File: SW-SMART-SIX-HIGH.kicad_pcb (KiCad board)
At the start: 2 copper layers, 107.7 x 76.2 mm, 97 parts, among them J1 SWLINK, J2 USART2, J3 POWER OUT, J4 POWER IN, J5 POWER OUT, SW0 BTS7002-1EPP, SW1 BTS7002-1EPP, SW2 BTS7002-1EPP, SW3 BTS7002-1EPP, SW4 BTS7002-1EPP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

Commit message: fine tune a few things
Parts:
- J1: value SWLINK -> SWD
- moved CIN2 6.40 mm to (94.2, 83.0), turned to 0 degrees
- moved CIN1 5.70 mm to (93.8, 85.4), turned to 0 degrees
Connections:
- C3V1 pad 1: +3.3V -> Net-(U4-Vio)
- D3 pad 2: /STAT2 -> unconnected-(D3-A-Pad2)
- U4 pad 5: +3.3V -> Net-(U4-Vio)
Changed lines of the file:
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@@
 	(net 132 "/STAT2")
 	(net 133 "Net-(D3-K)")
+	(net 134 "Net-(U4-Vio)")
+	(net 135 "unconnected-(D3-A-Pad2)")
 	(footprint "TerminalBlock_Phoenix:TerminalBlock_Phoenix_MKDS-3-5-5.08_1x05_P5.08mm_Horizontal"
 		(layer "F.Cu")
@@
 	(footprint "Capacitor_SMD:C_1210_3225Metric_Pad1.33x2.70mm_HandSolder"
 		(layer "F.Cu")
-		(at 90.95 80.4375 90)
+		(at 93.7625 85.4)
 		(descr "Capacitor SMD 1210 (3225 Metric), square (rectangular) end terminal, IPC-7351 nominal with elongated pad for handsoldering. (Body size source: IPC-SM-782 page 76, https://www.pcb-3d.com/wordpress/wp-content/uploads/ipc-sm-782a_amendment_1_and_2.pdf), generated with kicad-footprint-generator")
 		(tags "capacitor handsolder")
 		(property "Reference" "CIN1"
-			(at 4.1 0.2 90)
+			(at 0.375 2.2 0)
 			(layer "F.SilkS")
 			(effects
@@
 		)
 		(property "Value" "10u"
-			(at 0 2.3 90)
+			(at 0 2.3 0)
 			(layer "F.Fab")
 			(hide yes)
@@
 		)
 		(property "Datasheet" "~"
-			(at 0 0 90)
+			(at 0 0 0)
 			(layer "F.Fab")
 			(hide yes)
@@
 		)
 		(property "Description" "10uf / 50v"
-			(at 0 0 90)
+			(at 0 0 0)
 			(layer "F.Fab")
 			(hide yes)
@@
 		)
 		(fp_text user "${REFERENCE}"
-			(at 0 0 90)
+			(at 0 0 0)
 			(layer "F.Fab")
 			(effects
@@
 		)
 		(pad "1" smd roundrect
-			(at -1.5625 0 90)
+			(at -1.5625 0)
 			(size 1.325 2.7)
 			(layers "F.Cu" "F.Mask" "F.Paste")
@@
 		)
 		(pad "2" smd roundrect
-			(at 1.5625 0 90)
+			(at 1.5625 0)
 			(size 1.325 2.7)
 			(layers "F.Cu" "F.Mask" "F.Paste")
@@
 		(tags "LQFP QFP")
 		(property "Reference" "U1"
-			(at 0 -7.4 0)
+			(at -7.05 -4.7 0)
 			(layer "F.SilkS")
 			(effects
@@
 		(property "Value" "H GND L"
 			(at 5.035 5.683157 0)
-			(layer "F.Fab")
-			(hide yes)
+			(layer "F.SilkS")
 			(effects
 				(font
@@
 			(layers "F.Cu" "F.Mask" "F.Paste")
 			(roundrect_rratio 0.217391)
-			(net 132 "/STAT2")
+			(net 135 "unconnected-(D3-A-Pad2)")
 			(pinfunction "A")
 			(pintype "passive")
@@
 	(footprint "Capacitor_SMD:C_0603_1608Metric_Pad1.08x0.95mm_HandSolder"
 		(layer "F.Cu")
-		(at 88.55 80 90)
+		(at 94.2 83)
 		(descr "Capacitor SMD 0603 (1608 Metric), square (rectangular) end terminal, IPC-7351 nominal with elongated pad for handsoldering. (Body size source: IPC-SM-782 page 76, https://www.pcb-3d.com/wordpress/wp-content/uploads/ipc-sm-782a_amendment_1_and_2.pdf), generated with kicad-footprint-generator")
 		(tags "capacitor handsolder")
 		(property "Reference" "CIN2"
-			(at -0.0625 -1.1 90)
+			(at -0.0625 -1.3 0)
 			(layer "F.SilkS")
 			(effects
@@
 		)
 		(property "Value" "100n"
-			(at 0 1.43 90)
+			(at 0 1.43 0)
 			(layer "F.Fab")
 			(hide yes)
@@
 		)
 		(property "Datasheet" "~"
-			(at 0 0 90)
+			(at 0 0 0)
 			(layer "F.Fab")
 			(hide yes)
@@
 		)
 		(property "Description" "100n / 100v"
-			(at 0 0 90)
+			(at 0 0 0)
 			(layer "F.Fab")
 			(hide yes)
@@
 		)
 		(fp_text user "${REFERENCE}"
-			(at 0 0 90)
+			(at 0 0 0)
 			(layer "F.Fab")
 			(effects
@@
 		)
 		(pad "1" smd roundrect
-			(at -0.8625 0 90)
+			(at -0.8625 0)
 			(size 1.075 0.95)
 			(layers "F.Cu" "F.Mask" "F.Paste")
@@
 		)
 		(pad "2" smd roundrect
-			(at 0.8625 0 90)
+			(at 0.8625 0)
 			(size 1.075 0.95)
 			(layers "F.Cu" "F.Mask" "F.Paste")
@@
 			(layers "F.Cu" "F.Mask" "F.Paste")
 			(roundrect_rratio 0.25)
-			(net 2 "+3.3V")
+			(net 134 "Net-(U4-Vio)")
 			(pinfunction "Vio")
 			(pintype "power_in")
@@
 		)
 		(property "Value" "USART2"
-			(at 0 10 90)
-			(layer "F.Fab")
-			(hide yes)
+			(at 2.189843 3.97 180)
+			(layer "F.SilkS")
 			(effects
 				(font
@@
 			(layers "F.Cu" "F.Mask" "F.Paste")
 			(roundrect_rratio 0.25)
-			(net 2 "+3.3V")
+			(net 134 "Net-(U4-Vio)")
 			(pintype "passive")
 		)
@@
 			)
 		)
-		(property "Value" "SWLINK"
-			(at 0 12.54 90)
-			(layer "F.Fab")
-			(hide yes)
+		(property "Value" "SWD"
+			(at 2.189843 5.06 180)
+			(layer "F.SilkS")
 			(effects
 				(font
@@
 		(property "Value" "8.2 uH 55.2 mOhm"
 			(at 0 0 90)
-			(layer "F.Fab")
+			(layer "F.SilkS")
 			(hide yes)
 			(effects
@@
 	)
 	(via
-		(at 89.55 77.6375)
+		(at 96.5625 84)
 		(size 0.508)
 		(drill 0.254)
@@
 	)
 	(via
-		(at 88.65 78.1375)
+		(at 96.0625 83.1)
 		(size 0.508)
 		(drill 0.254)
@@
 	)
 	(via
-		(at 92.15 77.6375)
+		(at 96.5625 86.6)
 		(size 0.508)
 		(drill 0.254)
@@
 	)
 	(via
-		(at 90.75 77.6375)
+		(at 96.5625 85.2)
 		(size 0.508)
 		(drill 0.254)
@@
 	)
 	(via
-		(at 91.45 77.6375)
+		(at 96.5625 85.9)
 		(size 0.508)
 		(drill 0.254)
@@
 	)
 	(via
-		(at 88.95 77.6375)
+		(at 96.5625 83.4)
 		(size 0.508)
 		(drill 0.254)
@@
 	)
 	(via
-		(at 88.35 77.6375)
+		(at 96.5625 82.8)
 		(size 0.508)
 		(drill 0.254)
@@
 	)
 	(via
-		(at 90.15 77.6375)
+		(at 96.5625 84.6)
 		(size 0.508)
 		(drill 0.254)
@@
 		(polygon
 			(pts
-				(xy 92.55 79.7375) (xy 87.75 79.7375) (xy 87.75 77.3375) (xy 92.55 77.3375)
+				(xy 94.4625 87) (xy 94.4625 82.2) (xy 96.8625 82.2) (xy 96.8625 87)
 			)
 		)

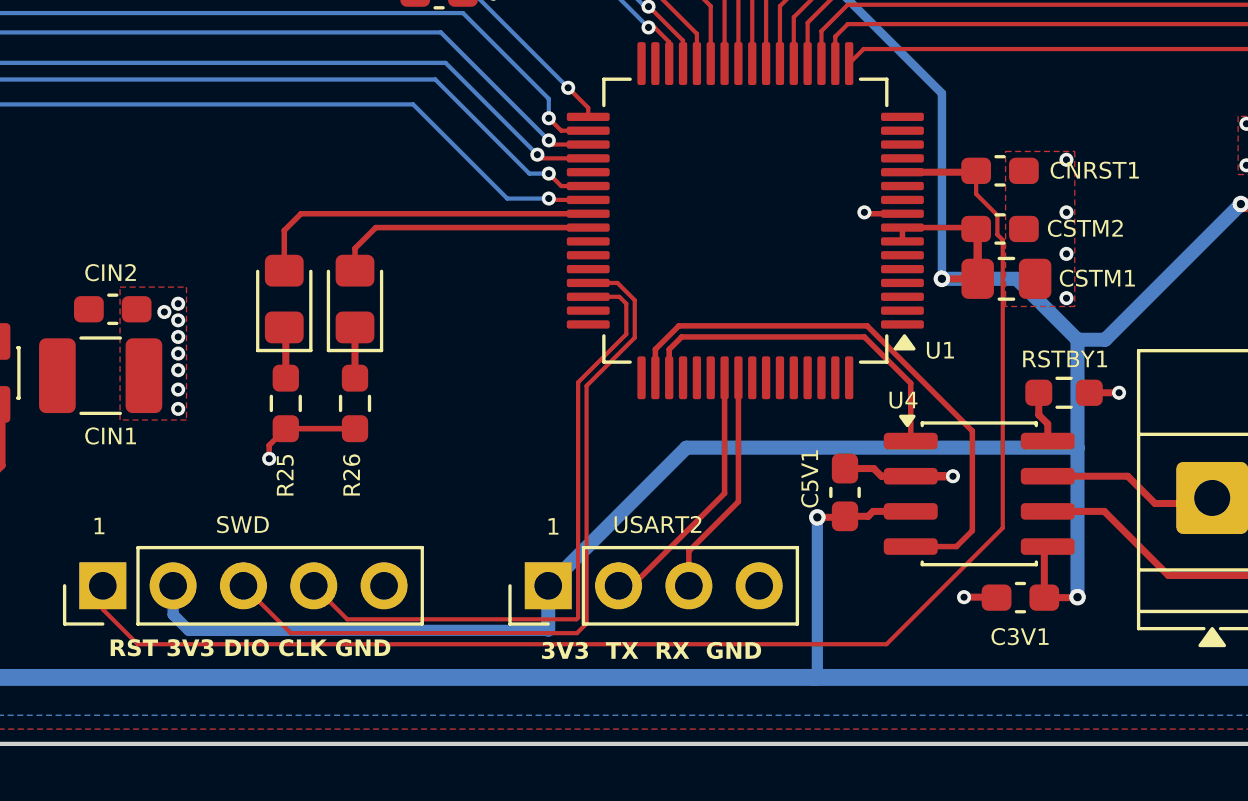
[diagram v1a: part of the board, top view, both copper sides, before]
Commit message: fix a few issues that cropped up
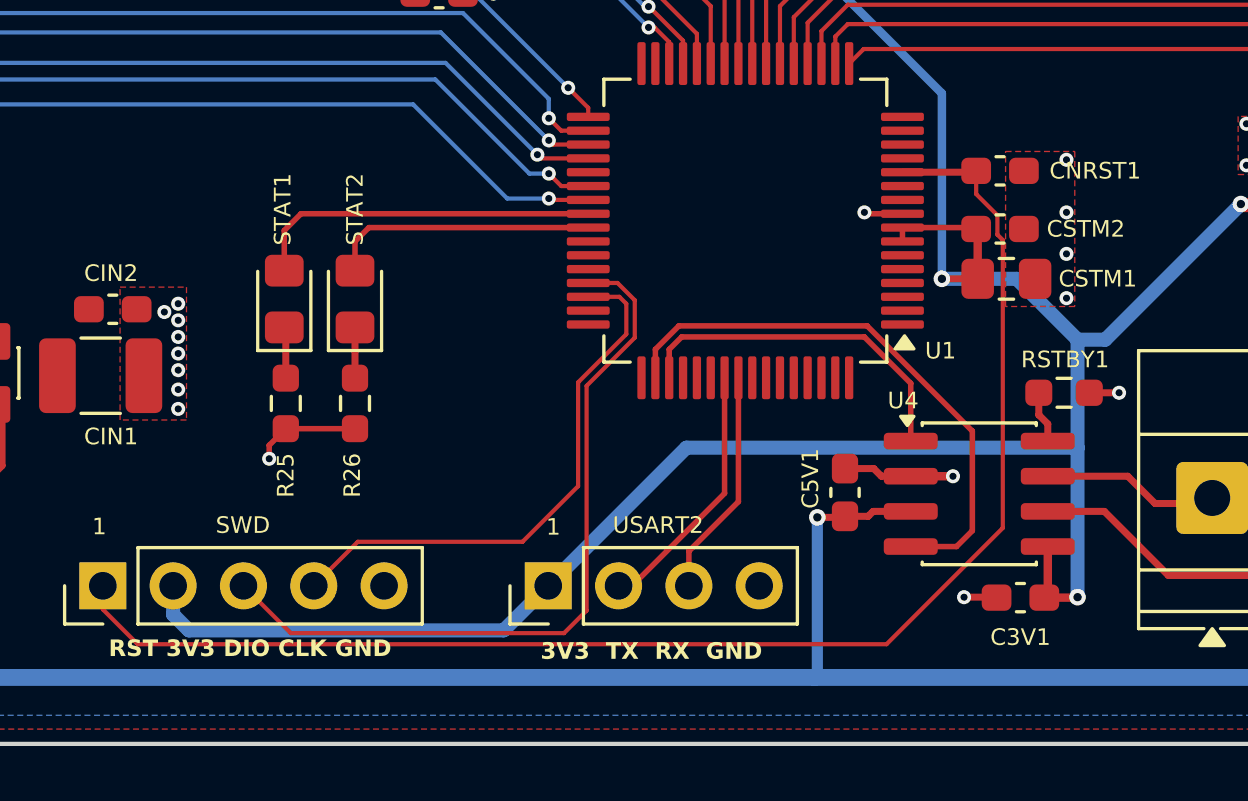
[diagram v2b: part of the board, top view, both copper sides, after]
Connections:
- C3V1 pad 1: Net-(U4-Vio) -> +3.3V
- D3 pad 2: unconnected-(D3-A-Pad2) -> /STAT2
- U4 pad 5: Net-(U4-Vio) -> +3.3V
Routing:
- net /SWCLK: track 23.6 -> 19.8 mm
- net +3.3V: track 110.2 -> 109.2 mm
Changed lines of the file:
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@@
 	(net 132 "/STAT2")
 	(net 133 "Net-(D3-K)")
-	(net 134 "Net-(U4-Vio)")
-	(net 135 "unconnected-(D3-A-Pad2)")
 	(footprint "TerminalBlock_Phoenix:TerminalBlock_Phoenix_MKDS-3-5-5.08_1x05_P5.08mm_Horizontal"
 		(layer "F.Cu")
@@
 		(property "Value" "STAT2"
 			(at 3.2425 0 90)
-			(layer "F.Fab")
-			(hide yes)
+			(layer "F.SilkS")
 			(effects
 				(font
@@
 			(layers "F.Cu" "F.Mask" "F.Paste")
 			(roundrect_rratio 0.217391)
-			(net 135 "unconnected-(D3-A-Pad2)")
+			(net 132 "/STAT2")
 			(pinfunction "A")
 			(pintype "passive")
@@
 			(layers "F.Cu" "F.Mask" "F.Paste")
 			(roundrect_rratio 0.25)
-			(net 134 "Net-(U4-Vio)")
+			(net 2 "+3.3V")
 			(pinfunction "Vio")
 			(pintype "power_in")
@@
 			(layers "F.Cu" "F.Mask" "F.Paste")
 			(roundrect_rratio 0.25)
-			(net 134 "Net-(U4-Vio)")
+			(net 2 "+3.3V")
 			(pintype "passive")
 		)
@@
 		(property "Value" "STAT1"
 			(at 3.2425 -0.055 90)
-			(layer "F.Fab")
-			(hide yes)
+			(layer "F.SilkS")
 			(effects
 				(font
@@
 	)
 	(segment
-		(start 127.85 93.416843)
-		(end 129.033157 93.416843)
-		(width 0.254)
-		(layer "F.Cu")
-		(net 2)
-	)
-	(segment
 		(start 105.8625 69.7375)
 		(end 105.8625 69.265)
@@
 	)
 	(segment
-		(start 122.725 80.55)
-		(end 122.725 80.05)
-		(width 0.2)
+		(start 127.85 93.416843)
+		(end 129.033157 93.416843)
+		(width 0.305)
 		(layer "F.Cu")
 		(net 2)
 	)
 	(segment
-		(start 127.85 93.416843)
-		(end 127.85 91.696843)
-		(width 0.254)
+		(start 122.725 80.55)
+		(end 122.725 80.05)
+		(width 0.2)
 		(layer "F.Cu")
 		(net 2)
@@
 	)
 	(segment
+		(start 129.033157 93.416843)
+		(end 129.05 93.4)
+		(width 0.305)
+		(layer "F.Cu")
+		(net 2)
+	)
+	(segment
 		(start 109.05 67.8)
 		(end 109.15 67.9)
@@
 	)
 	(segment
-		(start 108.05 67.8)
-		(end 106.4325 67.8)
-		(width 0.254)
+		(start 127.975 91.571843)
+		(end 127.975 93.291843)
+		(width 0.305)
 		(layer "F.Cu")
 		(net 2)
 	)
 	(segment
-		(start 129.033157 93.416843)
-		(end 129.05 93.4)
+		(start 108.05 67.8)
+		(end 106.4325 67.8)
 		(width 0.254)
 		(layer "F.Cu")
@@
 	)
 	(segment
+		(start 96.38 94.03)
+		(end 96.95 94.6)
+		(width 0.508)
+		(layer "B.Cu")
+		(net 2)
+	)
+	(segment
 		(start 124.15 75.2)
 		(end 124.15 81.9)
@@
 	)
 	(segment
-		(start 96.38 94.03)
-		(end 96.95 94.6)
-		(width 0.406)
-		(layer "B.Cu")
-		(net 2)
-	)
-	(segment
 		(start 126.85 81.9)
 		(end 129.05 84.1)
@@
 	)
 	(segment
-		(start 96.95 94.6)
-		(end 109.95 94.6)
-		(width 0.406)
+		(start 129.05 88)
+		(end 129.05 93.4)
+		(width 0.508)
 		(layer "B.Cu")
 		(net 2)
 	)
 	(segment
-		(start 129.05 88)
-		(end 129.05 93.4)
+		(start 96.95 94.6)
+		(end 108.319843 94.6)
 		(width 0.508)
 		(layer "B.Cu")
@@
 	)
 	(segment
-		(start 109.93 92.989843)
-		(end 109.93 94.58)
-		(width 0.508)
-		(layer "B.Cu")
-		(net 2)
-	)
-	(segment
-		(start 96.38 92.989843)
-		(end 96.38 94.03)
-		(width 0.406)
-		(layer "B.Cu")
-		(net 2)
-	)
-	(segment
 		(start 130.05 84.1)
 		(end 129.05 84.1)
@@
 	)
 	(segment
-		(start 109.93 94.58)
-		(end 109.95 94.6)
+		(start 110.95 69.5)
+		(end 118.45 69.5)
 		(width 0.305)
 		(layer "B.Cu")
@@
 	)
 	(segment
-		(start 110.95 69.5)
-		(end 118.45 69.5)
-		(width 0.305)
+		(start 96.38 92.989843)
+		(end 96.38 94.03)
+		(width 0.508)
 		(layer "B.Cu")
 		(net 2)
@@
 		(net 2)
 	)
+	(segment
+		(start 108.319843 94.6)
+		(end 109.93 92.989843)
+		(width 0.508)
+		(layer "B.Cu")
+		(net 2)
+	)
 	(via
 		(at 121.75 60.1)
@@
 	)
 	(segment
-		(start 112.5 82.55)
-		(end 111.375 82.55)
+		(start 101.46 92.989843)
+		(end 103.049843 91.4)
 		(width 0.1524)
 		(layer "F.Cu")
@@
 	)
 	(segment
-		(start 112.75 83.9)
-		(end 112.75 82.8)
+		(start 111.0096 89.3904)
+		(end 111.0096 85.6404)
 		(width 0.1524)
 		(layer "F.Cu")
@@
 	)
 	(segment
-		(start 102.670157 94.2)
-		(end 110.95 94.2)
+		(start 111.0096 85.6404)
+		(end 112.75 83.9)
 		(width 0.1524)
 		(layer "F.Cu")
@@
 	)
 	(segment
-		(start 112.75 82.8)
-		(end 112.5 82.55)
+		(start 112.5 82.55)
+		(end 111.375 82.55)
 		(width 0.1524)
 		(layer "F.Cu")
@@
 	)
 	(segment
-		(start 111.0096 85.6404)
-		(end 112.75 83.9)
+		(start 112.75 83.9)
+		(end 112.75 82.8)
 		(width 0.1524)
 		(layer "F.Cu")
@@
 	)
 	(segment
-		(start 101.46 92.989843)
-		(end 102.670157 94.2)
+		(start 112.75 82.8)
+		(end 112.5 82.55)
 		(width 0.1524)
 		(layer "F.Cu")
@@
 	)
 	(segment
-		(start 111.0096 94.1404)
-		(end 111.0096 85.6404)
+		(start 103.049843 91.4)
+		(end 109 91.4)
 		(width 0.1524)
 		(layer "F.Cu")
@@
 	)
 	(segment
-		(start 110.95 94.2)
-		(end 111.0096 94.1404)
+		(start 109 91.4)
+		(end 111.0096 89.3904)
 		(width 0.1524)
 		(layer "F.Cu")
@@
 	)
 	(segment
-		(start 111.3154 94.350833)
-		(end 111.3154 85.767066)
+		(start 110.5 94.7)
+		(end 111.3154 93.8846)
 		(width 0.1524)
 		(layer "F.Cu")
@@
 	)
 	(segment
-		(start 113.0558 82.673333)
-		(end 112.432467 82.05)
+		(start 112.432467 82.05)
+		(end 111.375 82.05)
 		(width 0.1524)
 		(layer "F.Cu")
@@
 	)
 	(segment
-		(start 112.432467 82.05)
-		(end 111.375 82.05)
+		(start 111.3154 93.8846)
+		(end 111.3154 85.767066)
 		(width 0.1524)
 		(layer "F.Cu")
@@
 	(segment
 		(start 100.630157 94.7)
-		(end 110.966233 94.7)
+		(end 110.5 94.7)
 		(width 0.1524)
 		(layer "F.Cu")
@@
 	)
 	(segment
-		(start 113.0558 84.026667)
-		(end 113.0558 82.673333)
+		(start 111.3154 85.767066)
+		(end 113.0558 84.026667)
 		(width 0.1524)
 		(layer "F.Cu")
@@
 	)
 	(segment
-		(start 110.966233 94.7)
-		(end 111.3154 94.350833)
+		(start 113.0558 82.673333)
+		(end 112.432467 82.05)
 		(width 0.1524)
 		(layer "F.Cu")
@@
 	)
 	(segment
-		(start 111.3154 85.767066)
-		(end 113.0558 84.026667)
+		(start 113.0558 84.026667)
+		(end 113.0558 82.673333)
 		(width 0.1524)
 		(layer "F.Cu")
@@
 	)
 	(segment
-		(start 102.95 80.8)
-		(end 103.7 80.05)
+		(start 103.45 80.05)
+		(end 102.95 80.55)
 		(width 0.2)
 		(layer "F.Cu")
@@
 	)
 	(segment
-		(start 103.7 80.05)
-		(end 111.375 80.05)
+		(start 102.95 80.55)
+		(end 102.95 81.60625)
 		(width 0.2)
 		(layer "F.Cu")
@@
 	)
 	(segment
-		(start 102.95 81.60625)
-		(end 102.95 80.8)
+		(start 111.375 80.05)
+		(end 103.45 80.05)
 		(width 0.2)
 		(layer "F.Cu")

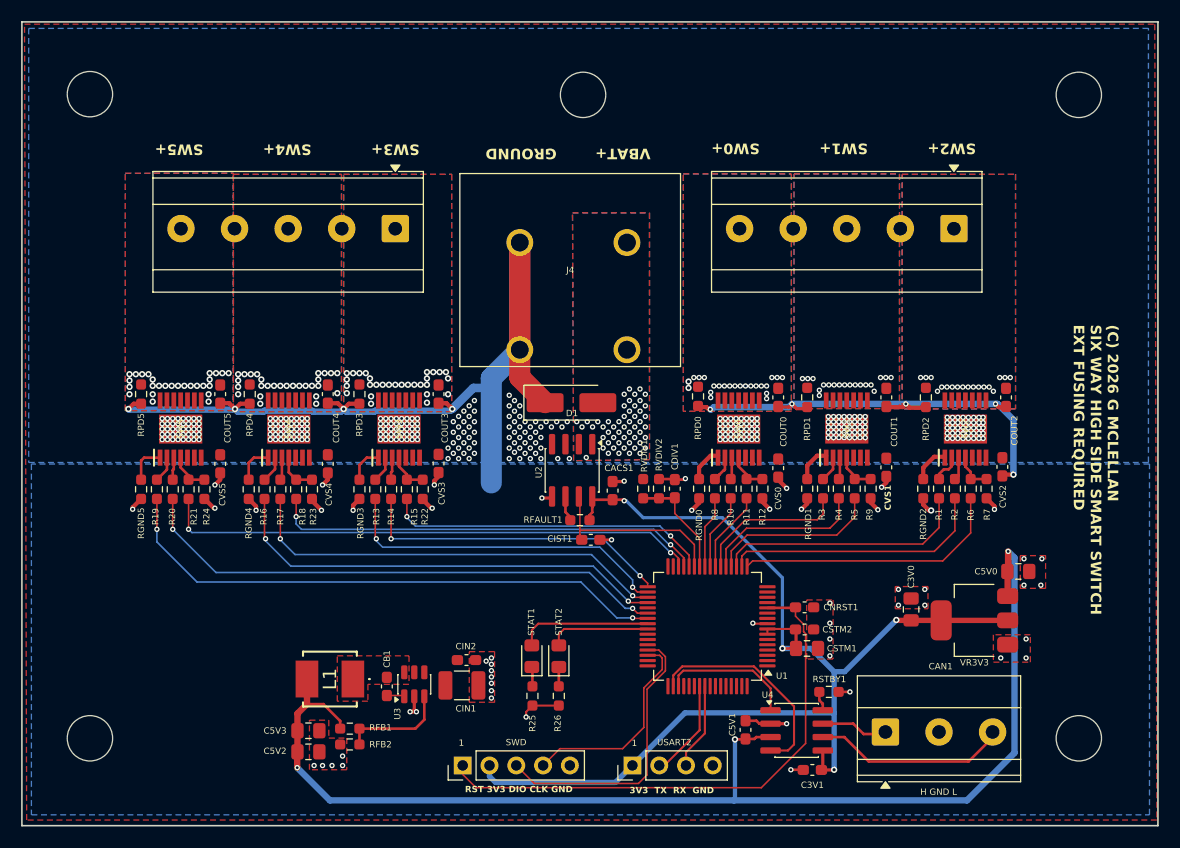
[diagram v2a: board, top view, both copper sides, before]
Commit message: added dedicated board temperature sensor
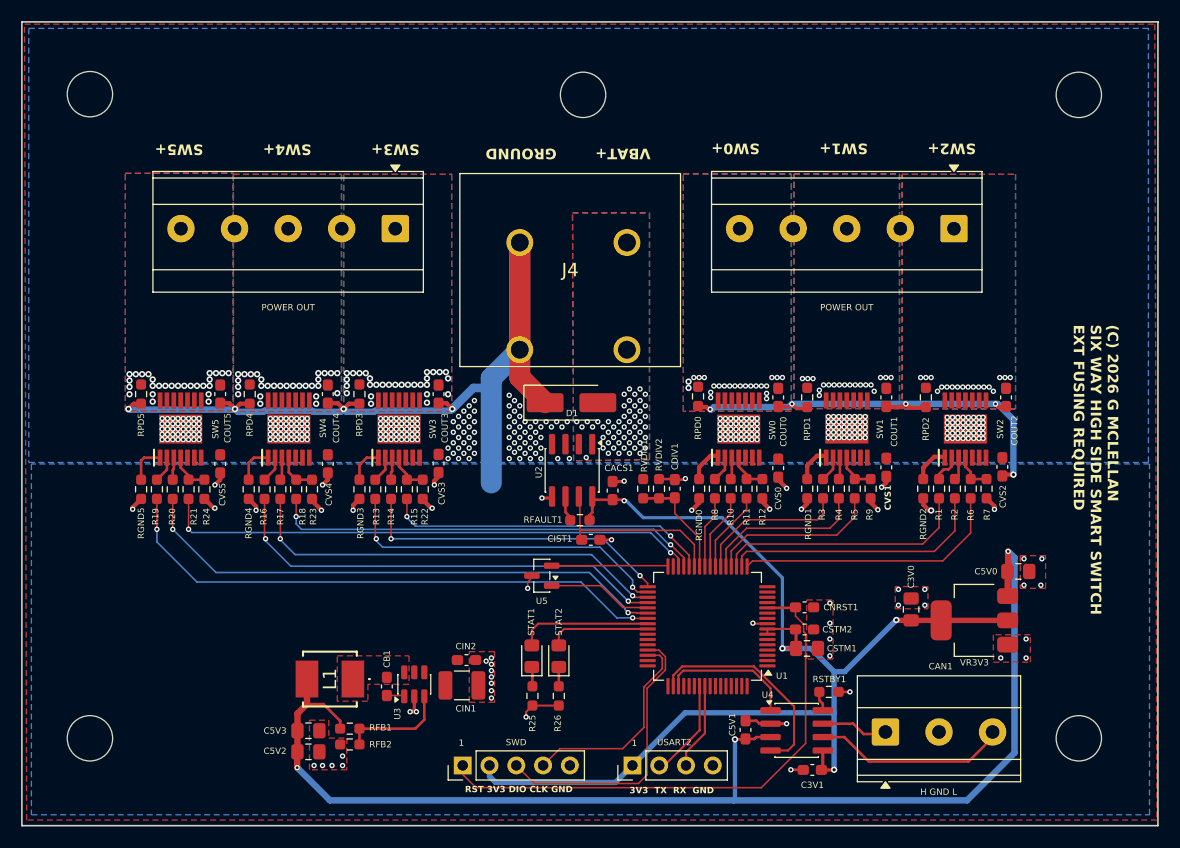
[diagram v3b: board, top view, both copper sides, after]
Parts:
- added U5: MCP9700Ax-ETT, Package_TO_SOT_SMD:SOT-23, F.Cu at (101.3, 75.0)
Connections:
- U1 pad 32: unconnected-(U1-PB12-Pad32) -> /BRDTMP
- U1 pad 37: unconnected-(U1-PA9/UCPD1_DBCC1-Pad37) -> /TMP_PWR
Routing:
- net /BRDTMP: track 0.00 -> 11.1 mm
- net /TMP_PWR: track 0.00 -> 9.97 mm
- net GND: track 172.4 -> 173.7 mm, vias 65 -> 66
